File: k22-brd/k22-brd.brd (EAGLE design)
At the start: 21.6 x 63.5 mm, 35 parts, among them J1 61302011121, J2 61302011121, J3 CORTEX_DEBUG_PTH

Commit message: Prvni verze shieldu
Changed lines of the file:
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@@
 <setting verticaltext="up"/>
 </settings>
-<grid distance="25" unitdist="mil" unit="mil" style="dots" multiple="1" display="yes" altdistance="6.25" altunitdist="mil" altunit="mil"/>
+<grid distance="12.5" unitdist="mil" unit="mil" style="dots" multiple="1" display="yes" altdistance="6.25" altunitdist="mil" altunit="mil"/>
 <layers>
 <layer number="1" name="Top" color="4" fill="1" visible="yes" active="yes"/>
@@
 <contactref element="J3" pad="4"/>
 <contactref element="J1" pad="11"/>
-<wire x1="4.1275" y1="16.8275" x2="6.6675" y2="19.3675" width="0.1524" layer="16"/>
-<wire x1="4.1275" y1="6.985" x2="4.1275" y2="16.8275" width="0.1524" layer="16"/>
-<wire x1="6.6675" y1="19.3675" x2="6.6675" y2="20.6375" width="0.1524" layer="16"/>
+<wire x1="4.1275" y1="16.51" x2="6.6675" y2="19.05" width="0.1524" layer="16"/>
+<wire x1="4.1275" y1="6.985" x2="4.1275" y2="16.51" width="0.1524" layer="16"/>
+<wire x1="6.6675" y1="19.05" x2="6.6675" y2="20.6375" width="0.1524" layer="16"/>
 <wire x1="6.6675" y1="20.6375" x2="5.3975" y2="21.9075" width="0.1524" layer="16"/>
 <via x="5.3975" y="21.9075" extent="1-16" drill="0.3"/>
@@
 <contactref element="J3" pad="2"/>
 <contactref element="RS2" pad="2"/>
-<wire x1="8.320125" y1="22.499465625" x2="6.032446875" y2="20.2117875" width="0.1524" layer="1"/>
-<wire x1="6.032446875" y1="20.2117875" x2="6.0325" y2="19.20875" width="0.1524" layer="1"/>
+<wire x1="8.320125" y1="22.499465625" x2="6.0324625" y2="20.211803125" width="0.1524" layer="1"/>
+<wire x1="6.0324625" y1="20.211803125" x2="6.0325" y2="19.52625" width="0.1524" layer="1"/>
 <contactref element="J1" pad="12"/>
-<via x="6.0325" y="19.20875" extent="1-16" drill="0.3"/>
-<wire x1="6.0325" y1="19.20875" x2="4.1275" y2="19.20875" width="0.1524" layer="16"/>
+<via x="6.0325" y="19.52625" extent="1-16" drill="0.3"/>
+<wire x1="6.0325" y1="19.52625" x2="4.445" y2="19.52625" width="0.1524" layer="16"/>
+<wire x1="4.445" y1="19.52625" x2="4.1275" y2="19.20875" width="0.1524" layer="16"/>
 <via x="4.1275" y="19.20875" extent="1-16" drill="0.3"/>
 <wire x1="4.1275" y1="19.20875" x2="3.4925" y2="19.84375" width="0.1524" layer="1"/>

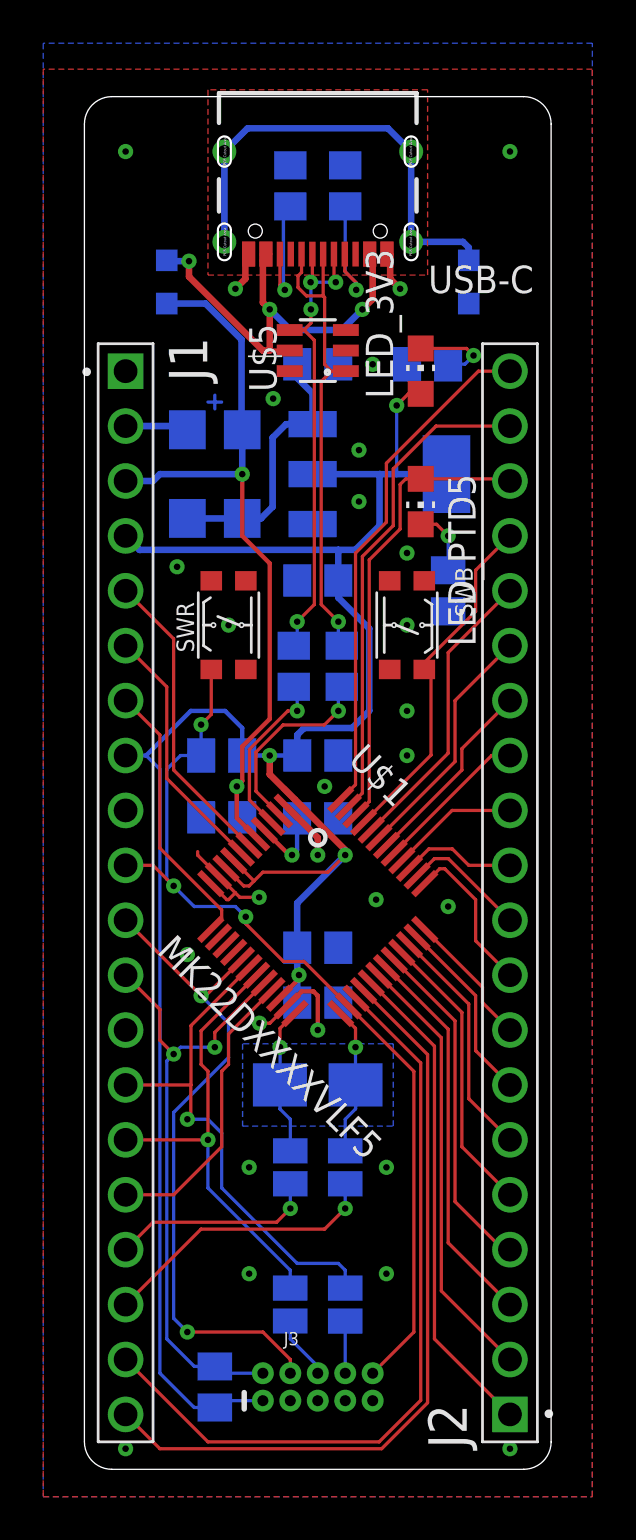
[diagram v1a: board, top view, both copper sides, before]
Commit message: overlap, crystal pad, usb pad, bead pad
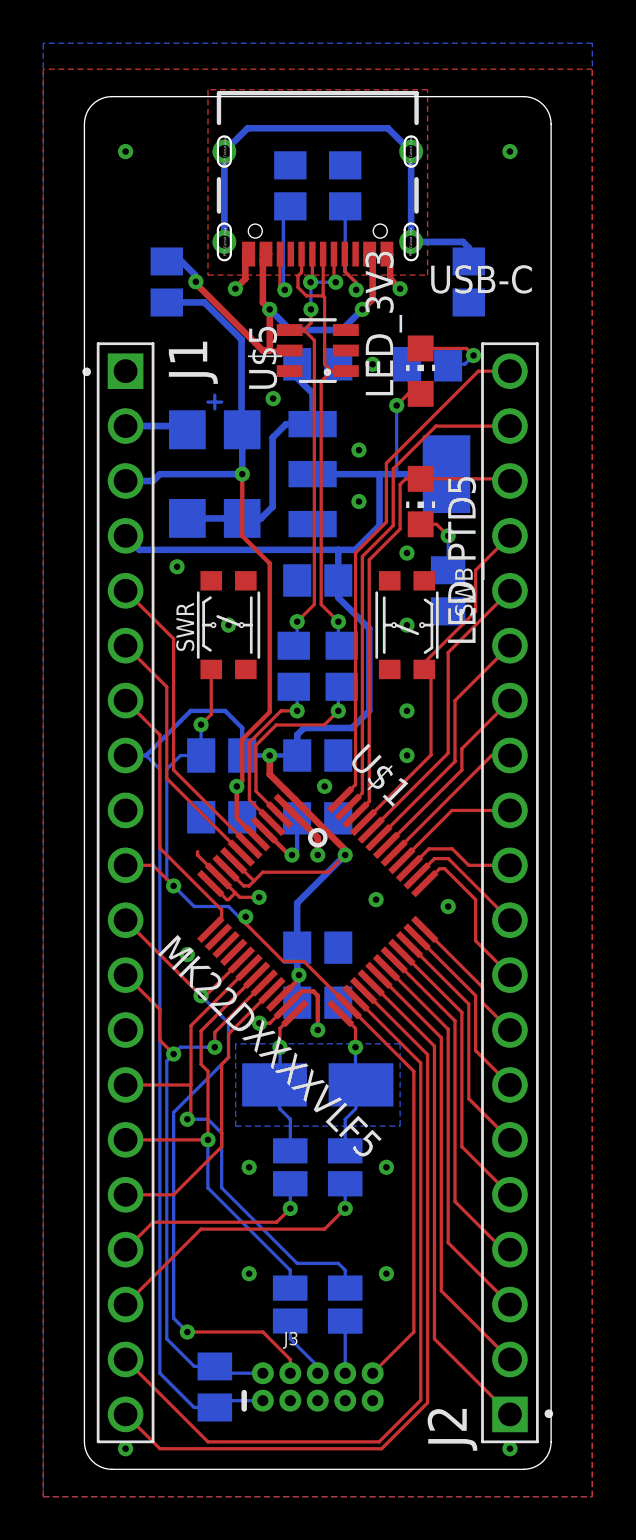
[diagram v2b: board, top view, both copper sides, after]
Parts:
- removed LU1, LU2: 330, rcl:L2012C
- added FBU1, FBU2: 330, BeagleBone_Black_Wireless:GHI-BASICCOMPONENTS_0805-RESISTOR
- USB-C: device Eagle_WR-USB (rev22b):629722000214 -> poli-USB-C:629722000214
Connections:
- net GND: now also FBU2.2; no longer LU2.1
- net USB5V: now also FBU1.2; no longer LU1.1
- net USBGNDSHIELD: now also FBU2.1; no longer LU2.2
- net VBUSCON: now also FBU1.1; no longer LU1.2

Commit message: Text v medi na spodni vrstve K22 desky
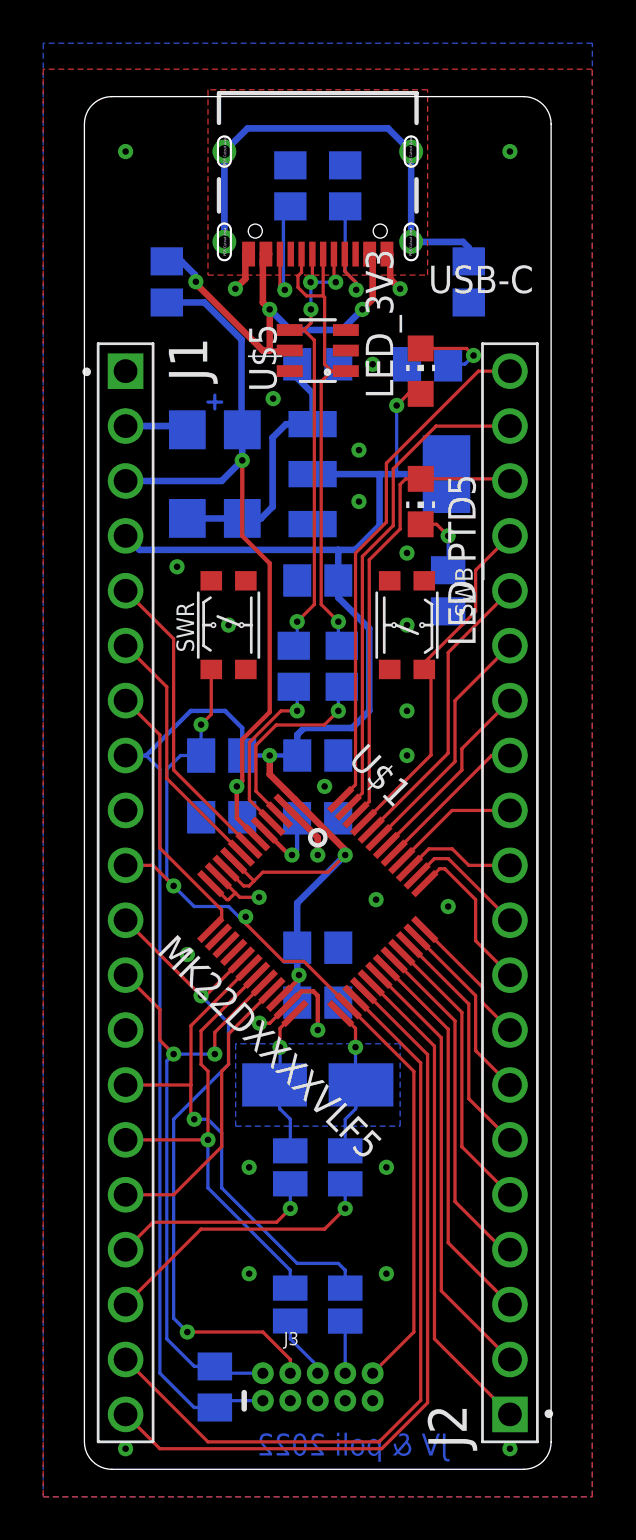
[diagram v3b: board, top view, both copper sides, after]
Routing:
- net GND: track 17.4 -> 15.8 mm
